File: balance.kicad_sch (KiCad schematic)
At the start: 5 parts, among them Q1 AO3400A

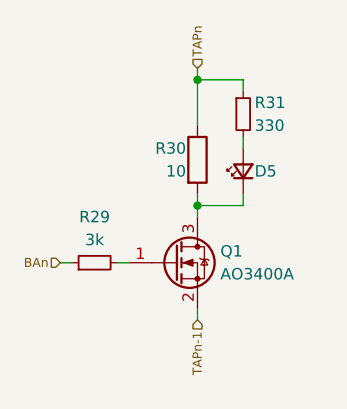
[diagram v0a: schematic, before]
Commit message: *: Remove thermistor protection zener diodes
Closes GH-8
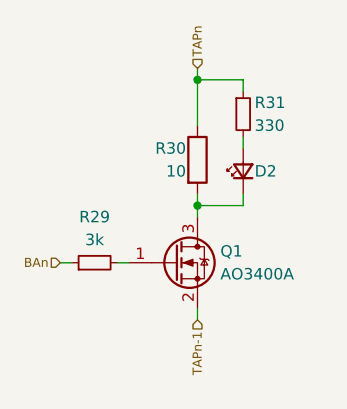
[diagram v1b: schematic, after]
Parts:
- renumbered D5 to D2
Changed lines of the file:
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@@
 		(on_board yes)
 		(dnp no)
-		(property "Reference" "D5"
+		(property "Reference" "D2"
 			(at 138.43 52.07 90)
 			(effects
@@
 			(project "bms"
 				(path "/ae4a7653-8e6d-4e05-b144-1e5e3b2092b7/28948f48-ac92-4ccf-aa29-40bfebbeebe0/061afbf0-38a7-4aad-9e58-d0f3974685d1"
+					(reference "D2")
+					(unit 1)
+				)
+				(path "/ae4a7653-8e6d-4e05-b144-1e5e3b2092b7/28948f48-ac92-4ccf-aa29-40bfebbeebe0/1868e0df-f8a0-46bd-9798-d286e5ba1ced"
+					(reference "D10")
+					(unit 1)
+				)
+				(path "/ae4a7653-8e6d-4e05-b144-1e5e3b2092b7/28948f48-ac92-4ccf-aa29-40bfebbeebe0/27f767ba-99fc-42f7-9230-5c46d6dfd697"
+					(reference "D6")
+					(unit 1)
+				)
+				(path "/ae4a7653-8e6d-4e05-b144-1e5e3b2092b7/28948f48-ac92-4ccf-aa29-40bfebbeebe0/4bc6a671-e3fb-4a27-8305-5f5b740fdf33"
+					(reference "D9")
+					(unit 1)
+				)
+				(path "/ae4a7653-8e6d-4e05-b144-1e5e3b2092b7/28948f48-ac92-4ccf-aa29-40bfebbeebe0/558077c3-2e79-4c16-bf32-75cbb22e7b66"
+					(reference "D12")
+					(unit 1)
+				)
+				(path "/ae4a7653-8e6d-4e05-b144-1e5e3b2092b7/28948f48-ac92-4ccf-aa29-40bfebbeebe0/5bcaf29d-feaf-497c-b526-6322a79bf7a6"
+					(reference "D11")
+					(unit 1)
+				)
+				(path "/ae4a7653-8e6d-4e05-b144-1e5e3b2092b7/28948f48-ac92-4ccf-aa29-40bfebbeebe0/8f62a6b1-c799-4e02-ae4e-ff12c4091a5b"
+					(reference "D3")
+					(unit 1)
+				)
+				(path "/ae4a7653-8e6d-4e05-b144-1e5e3b2092b7/28948f48-ac92-4ccf-aa29-40bfebbeebe0/a578400a-9630-406e-afcf-66a88224a81d"
+					(reference "D4")
+					(unit 1)
+				)
+				(path "/ae4a7653-8e6d-4e05-b144-1e5e3b2092b7/28948f48-ac92-4ccf-aa29-40bfebbeebe0/ae51574f-61f5-40a8-84a4-f02d08755389"
+					(reference "D13")
+					(unit 1)
+				)
+				(path "/ae4a7653-8e6d-4e05-b144-1e5e3b2092b7/28948f48-ac92-4ccf-aa29-40bfebbeebe0/b9f63902-5414-42f0-b092-c310bdd721ff"
+					(reference "D7")
+					(unit 1)
+				)
+				(path "/ae4a7653-8e6d-4e05-b144-1e5e3b2092b7/28948f48-ac92-4ccf-aa29-40bfebbeebe0/bc2a692e-3b59-4639-8552-ded9a92bfb3a"
 					(reference "D5")
 					(unit 1)
 				)
-				(path "/ae4a7653-8e6d-4e05-b144-1e5e3b2092b7/28948f48-ac92-4ccf-aa29-40bfebbeebe0/1868e0df-f8a0-46bd-9798-d286e5ba1ced"
-					(reference "D13")
-					(unit 1)
-				)
-				(path "/ae4a7653-8e6d-4e05-b144-1e5e3b2092b7/28948f48-ac92-4ccf-aa29-40bfebbeebe0/27f767ba-99fc-42f7-9230-5c46d6dfd697"
-					(reference "D9")
-					(unit 1)
-				)
-				(path "/ae4a7653-8e6d-4e05-b144-1e5e3b2092b7/28948f48-ac92-4ccf-aa29-40bfebbeebe0/4bc6a671-e3fb-4a27-8305-5f5b740fdf33"
-					(reference "D12")
-					(unit 1)
-				)
-				(path "/ae4a7653-8e6d-4e05-b144-1e5e3b2092b7/28948f48-ac92-4ccf-aa29-40bfebbeebe0/558077c3-2e79-4c16-bf32-75cbb22e7b66"
-					(reference "D15")
-					(unit 1)
-				)
-				(path "/ae4a7653-8e6d-4e05-b144-1e5e3b2092b7/28948f48-ac92-4ccf-aa29-40bfebbeebe0/5bcaf29d-feaf-497c-b526-6322a79bf7a6"
-					(reference "D14")
-					(unit 1)
-				)
-				(path "/ae4a7653-8e6d-4e05-b144-1e5e3b2092b7/28948f48-ac92-4ccf-aa29-40bfebbeebe0/8f62a6b1-c799-4e02-ae4e-ff12c4091a5b"
-					(reference "D6")
-					(unit 1)
-				)
-				(path "/ae4a7653-8e6d-4e05-b144-1e5e3b2092b7/28948f48-ac92-4ccf-aa29-40bfebbeebe0/a578400a-9630-406e-afcf-66a88224a81d"
-					(reference "D7")
-					(unit 1)
-				)
-				(path "/ae4a7653-8e6d-4e05-b144-1e5e3b2092b7/28948f48-ac92-4ccf-aa29-40bfebbeebe0/ae51574f-61f5-40a8-84a4-f02d08755389"
-					(reference "D16")
-					(unit 1)
-				)
-				(path "/ae4a7653-8e6d-4e05-b144-1e5e3b2092b7/28948f48-ac92-4ccf-aa29-40bfebbeebe0/b9f63902-5414-42f0-b092-c310bdd721ff"
-					(reference "D10")
-					(unit 1)
-				)
-				(path "/ae4a7653-8e6d-4e05-b144-1e5e3b2092b7/28948f48-ac92-4ccf-aa29-40bfebbeebe0/bc2a692e-3b59-4639-8552-ded9a92bfb3a"
+				(path "/ae4a7653-8e6d-4e05-b144-1e5e3b2092b7/28948f48-ac92-4ccf-aa29-40bfebbeebe0/c3623945-7d17-46cb-9ed3-2ec9fb31686f"
 					(reference "D8")
 					(unit 1)
 				)
-				(path "/ae4a7653-8e6d-4e05-b144-1e5e3b2092b7/28948f48-ac92-4ccf-aa29-40bfebbeebe0/c3623945-7d17-46cb-9ed3-2ec9fb31686f"
-					(reference "D11")
-					(unit 1)
-				)

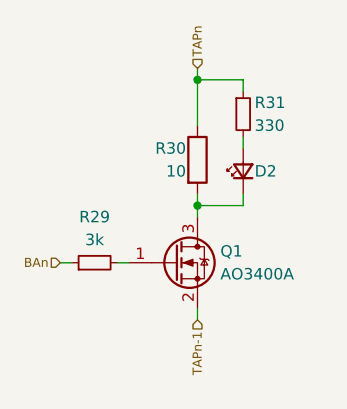
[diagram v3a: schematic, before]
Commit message: *: Use IRLML0060 for the balance MOSFETs
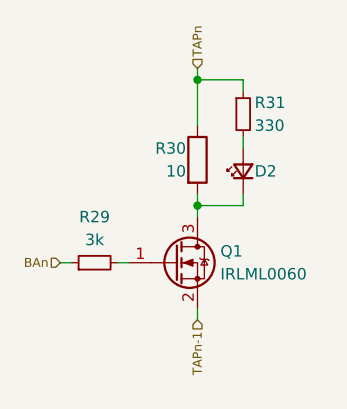
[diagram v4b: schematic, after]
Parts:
- Q1: value AO3400A -> IRLML0060; symbol Transistor_FET:AO3400A -> bms:IRLML0060; Dist # C347475 -> C67274; Mfr UMW -> Infineon; Mfr # AO3400A -> IRLML0060TRPBF
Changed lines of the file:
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@@
 	)
 	(symbol
-		(lib_id "Transistor_FET:AO3400A")
+		(lib_id "bms:IRLML0060")
 		(at 129.54 62.23 0)
 		(unit 1)
@@
 			)
 		)
-		(property "Value" "AO3400A"
+		(property "Value" "IRLML0060"
 			(at 134.62 63.5 0)
 			(effects
@@
 			)
 		)
-		(property "Datasheet" "http://www.aosmd.com/pdfs/datasheet/AO3400A.pdf"
+		(property "Datasheet" "https://www.infineon.com/dgdl/irlml0060pbf.pdf?fileId=5546d462533600a40153566493ef25e6"
 			(at 134.62 66.04 0)
 			(effects
@@
 			)
 		)
-		(property "Description" "30V Vds, 5.7A Id, N-Channel MOSFET, SOT-23"
+		(property "Description" "2.7A Id, 60V Vds, 92mOhm Rds, N-Channel HEXFET Power MOSFET, SOT-23"
 			(at 129.54 62.23 0)
 			(effects
@@
 			)
 		)
-		(property "Dist #" "C347475"
+		(property "Dist #" "C67274"
 			(at 129.54 62.23 0)
 			(effects
@@
 			)
 		)
-		(property "Mfr" "UMW"
+		(property "Mfr" "Infineon"
 			(at 129.54 62.23 0)
 			(effects
@@
 			)
 		)
-		(property "Mfr #" "AO3400A"
+		(property "Mfr #" "IRLML0060TRPBF"
 			(at 129.54 62.23 0)
 			(effects
